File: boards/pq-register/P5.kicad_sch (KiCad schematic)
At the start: 64 parts, among them Q30 T1-N652, Q31 T1-N652, Q33 T1-N652, Q34 T1-N652, Q35 T1-N652, Q36 T1-N652, Q37 T1-N652, Q50 T1-N652

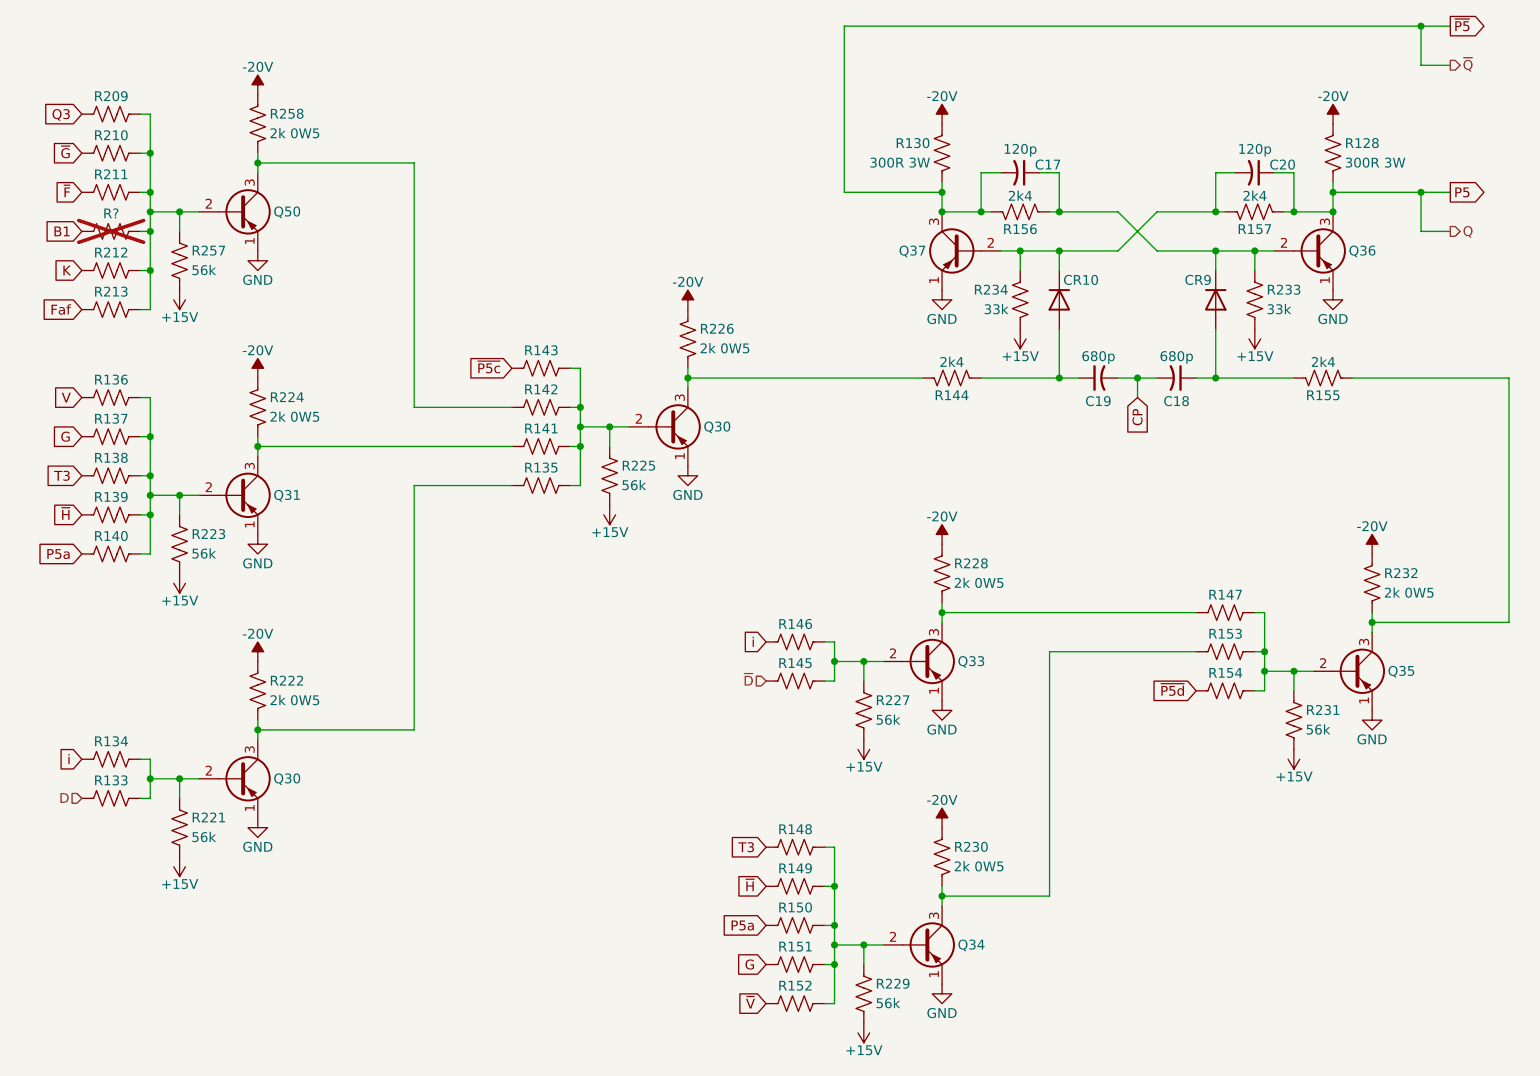
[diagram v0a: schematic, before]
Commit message: Run ERC and clean up P & Q Register board.
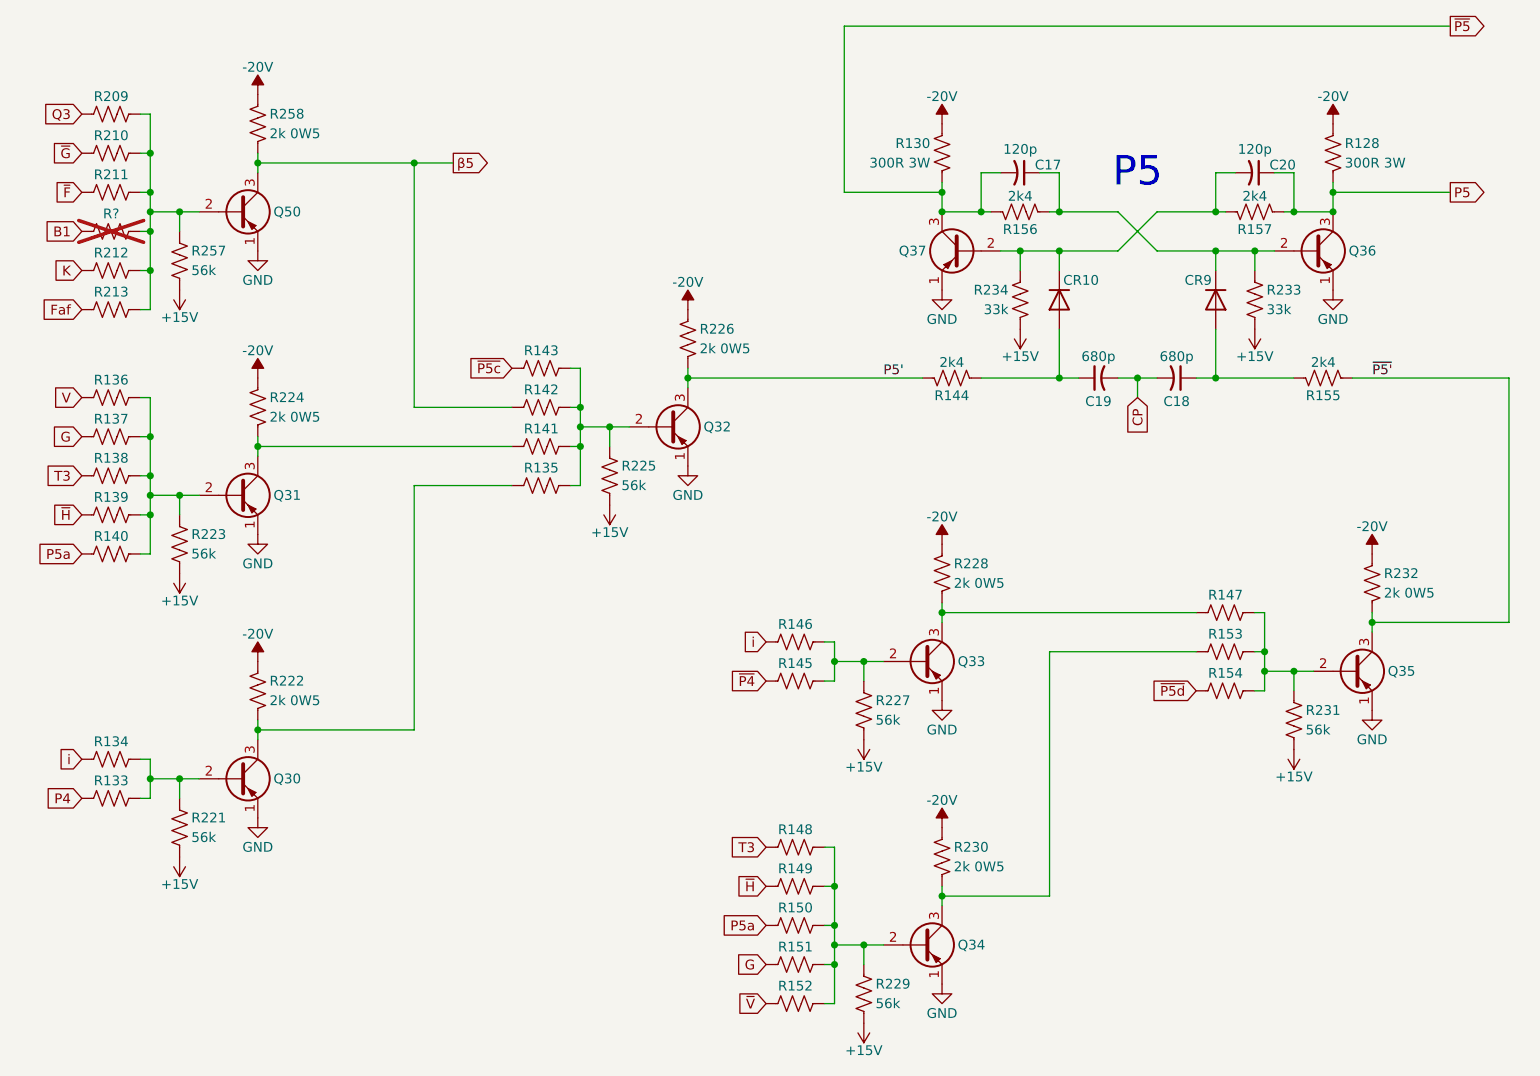
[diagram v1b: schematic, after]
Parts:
- renumbered Q30 to Q32
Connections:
- net ~{P5'}: now reaches Q35.3 (C), R155.2, R232.2
- net β5: now reaches Q50.3 (C), R142.1, R258.2
- net P5': now reaches Q32.3 (C), R144.1, R226.2
- net D renamed P4
- net ~{D} renamed ~{P4}
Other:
- note added: "P5"
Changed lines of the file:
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@@
 		(title "LGP-21 P & Q Register Board")
 	)
+	(text "P5"
+		(exclude_from_sim no)
+		(at 177.8 44.45 0)
+		(effects
+			(font
+				(size 3.81 3.81)
+			)
+		)
+	)
 	(junction
 		(at 49.53 83.82)
@@
 	)
 	(junction
+		(at 83.82 43.18)
+		(diameter 0)
+		(color 0 0 0 0)
+	)
+	(junction
 		(at 49.53 88.9)
 		(diameter 0)
@@
 	)
 	(junction
-		(at 214.63 25.4)
-		(diameter 0)
-		(color 0 0 0 0)
-	)
-	(junction
 		(at 49.53 86.36)
 		(diameter 0)
@@
 	)
 	(junction
-		(at 214.63 46.99)
-		(diameter 0)
-		(color 0 0 0 0)
-	)
-	(junction
 		(at 187.96 49.53)
 		(diameter 0)
@@
 	(wire
 		(pts
-			(xy 137.16 105.41) (xy 138.43 105.41)
-		)
-		(stroke
-			(width 0)
-			(type default)
-		)
-	)
-	(wire
-		(pts
-			(xy 137.16 137.16) (xy 138.43 137.16)
+			(xy 83.82 43.18) (xy 88.9 43.18)
 		)
 		(stroke
@@
 	(wire
 		(pts
-			(xy 49.53 57.15) (xy 49.53 52.07)
+			(xy 137.16 105.41) (xy 138.43 105.41)
 		)
 		(stroke
@@
 	(wire
 		(pts
-			(xy 203.2 45.72) (xy 203.2 46.99)
+			(xy 137.16 137.16) (xy 138.43 137.16)
 		)
 		(stroke
@@
 	(wire
 		(pts
-			(xy 194.31 109.22) (xy 198.12 109.22)
+			(xy 49.53 57.15) (xy 49.53 52.07)
 		)
 		(stroke
@@
 	(wire
 		(pts
-			(xy 218.44 25.4) (xy 214.63 25.4)
+			(xy 203.2 45.72) (xy 203.2 46.99)
 		)
 		(stroke
@@
 	(wire
 		(pts
-			(xy 218.44 30.48) (xy 214.63 30.48)
+			(xy 194.31 109.22) (xy 198.12 109.22)
 		)
 		(stroke
@@
 	(wire
 		(pts
-			(xy 214.63 46.99) (xy 218.44 46.99)
-		)
-		(stroke
-			(width 0)
-			(type default)
-		)
-	)
-	(wire
-		(pts
 			(xy 83.82 43.18) (xy 63.5 43.18)
 		)
@@
 	(wire
 		(pts
-			(xy 214.63 30.48) (xy 214.63 25.4)
-		)
-		(stroke
-			(width 0)
-			(type default)
-		)
-	)
-	(wire
-		(pts
 			(xy 205.74 71.12) (xy 226.06 71.12)
 		)
@@
 	(wire
 		(pts
-			(xy 218.44 52.07) (xy 214.63 52.07)
-		)
-		(stroke
-			(width 0)
-			(type default)
-		)
-	)
-	(wire
-		(pts
 			(xy 63.5 78.74) (xy 63.5 80.01)
 		)
@@
 	(wire
 		(pts
-			(xy 214.63 25.4) (xy 139.7 25.4)
+			(xy 139.7 25.4) (xy 218.44 25.4)
 		)
 		(stroke
@@
 	(wire
 		(pts
-			(xy 203.2 46.99) (xy 214.63 46.99)
+			(xy 203.2 46.99) (xy 218.44 46.99)
 		)
 		(stroke
@@
 	(wire
 		(pts
-			(xy 214.63 52.07) (xy 214.63 46.99)
-		)
-		(stroke
-			(width 0)
-			(type default)
-		)
-	)
-	(wire
-		(pts
 			(xy 142.24 147.32) (xy 142.24 144.78)
 		)
@@
 		)
 	)
+	(label "P5'"
+		(at 144.78 71.12 0)
+		(effects
+			(font
+				(size 1.27 1.27)
+			)
+			(justify left bottom)
+		)
+	)
+	(label "~{P5'}"
+		(at 208.28 71.12 0)
+		(effects
+			(font
+				(size 1.27 1.27)
+			)
+			(justify left bottom)
+		)
+	)
 	(global_label "T3"
 		(shape input)
@@
 		)
 	)
+	(global_label "P4"
+		(shape input)
+		(at 40.64 125.73 180)
+		(fields_autoplaced yes)
+		(effects
+			(font
+				(size 1.27 1.27)
+			)
+			(justify right)
+		)
+		(property "Intersheetrefs" "${INTERSHEET_REFS}"
+			(at 35.1753 125.73 0)
+			(hide yes)
+			(show_name no)
+			(do_not_autoplace no)
+			(effects
+				(font
+					(size 1.27 1.27)
+				)
+				(justify right)
+			)
+		)
+	)
 	(global_label "B1"
 		(shape input)
@@
 		)
 	)
+	(global_label "~{P4}"
+		(shape input)
+		(at 129.54 110.49 180)
+		(fields_autoplaced yes)
+		(effects
+			(font
+				(size 1.27 1.27)
+			)
+			(justify right)
+		)
+		(property "Intersheetrefs" "${INTERSHEET_REFS}"
+			(at 124.0753 110.49 0)
+			(hide yes)
+			(show_name no)
+			(do_not_autoplace no)
+			(effects
+				(font
+					(size 1.27 1.27)
+				)
+				(justify right)
+			)
+		)
+	)
 	(global_label "G"
 		(shape input)
@@
 		)
 	)
+	(global_label "β5"
+		(shape output)
+		(at 88.9 43.18 0)
+		(fields_autoplaced yes)
+		(effects
+			(font
+				(size 1.27 1.27)
+			)
+			(justify left)
+		)
+		(property "Intersheetrefs" "${INTERSHEET_REFS}"
+			(at 94.2437 43.18 0)
+			(hide yes)
+			(show_name no)
+			(do_not_autoplace no)
+			(effects
+				(font
+					(size 1.27 1.27)
+				)
+				(justify left)
+			)
+		)
+	)
 	(global_label "~{P5d}"
 		(shape input)
@@
 		)
 	)
-	(hierarchical_label "D"
-		(shape input)
-		(at 40.64 125.73 180)
-		(effects
-			(font
-				(size 1.27 1.27)
-			)
-			(justify right)
-		)
-	)
-	(hierarchical_label "~{D}"
-		(shape input)
-		(at 129.54 110.49 180)
-		(effects
-			(font
-				(size 1.27 1.27)
-			)
-			(justify right)
-		)
-	)
-	(hierarchical_label "~{Q}"
-		(shape output)
-		(at 218.44 30.48 0)
-		(effects
-			(font
-				(size 1.27 1.27)
-			)
-			(justify left)
-		)
-	)
-	(hierarchical_label "Q"
-		(shape output)
-		(at 218.44 52.07 0)
-		(effects
-			(font
-				(size 1.27 1.27)
-			)
-			(justify left)
-		)
-	)
 	(symbol
 		(lib_id "Device:R_US")
@@
 		(in_pos_files yes)
 		(dnp no)
-		(property "Reference" "Q30"
+		(property "Reference" "Q32"
 			(at 121.412 77.47 0)
 			(show_name no)
@@
 			(project "pq-register"
 				(path "/d5da316c-1ec9-4d99-8330-1c4a3f6c3ba4/57c22bd7-5c59-41f0-a879-47621ba4147d"
-					(reference "Q30")
+					(reference "Q32")
 					(unit 1)
 				)

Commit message: Add copyright information.
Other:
- company: (none) -> © 1962 General Precision; redrawn by Sam Hanes
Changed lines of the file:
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@@
 	(title_block
 		(title "LGP-21 P & Q Register Board")
+		(date "2026-06-15")
+		(rev "ESD 1060")
+		(company "© 1962 General Precision; redrawn by Sam Hanes")
+		(comment 1 "https://github.com/Elemecca/lgp21-docs")
 	)
 	(text "P5"
